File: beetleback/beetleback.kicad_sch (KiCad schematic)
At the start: 12 parts, among them J1 Conn_01x01_Male, J2 Conn_01x03_Male, J3 Conn_01x01_Male, U1 TA6586, U2 ATtiny412-SS, U3 ME6214A33M3G

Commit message: beetle motor esc back
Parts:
- removed C3: 10uF, Capacitor_SMD:C_0805_2012Metric, symbol Device:C
- removed D1: LED, LED_SMD:LED_0603_1608Metric_Castellated, symbol Device:LED
- removed J1, J3: Conn_01x01_Male, Connector_Wire:SolderWire-2sqmm_1x01_D2mm_OD3.9mm, symbol Connector:Conn_01x01_Male
- removed R1, R2: 330R, Resistor_SMD:R_0603_1608Metric, symbol Device:R
- removed U1: TA6586, Package_DIP:DIP-8_W7.62mm, symbol beetleback:TA6586
- removed U2: ATtiny412-SS, Package_SO:SOIC-8_3.9x4.9mm_P1.27mm, symbol MCU_Microchip_ATtiny:ATtiny412-SS
- removed U3: ME6214A33M3G, Package_TO_SOT_SMD:SOT-23, symbol beetleback:ME6214A33M3G
- added C5, C6, C7, C8: 22uF 18v, Capacitor_SMD:C_1206_3216Metric, symbol Device:C
- added C9: 1uF, Capacitor_SMD:C_0603_1608Metric, symbol Device:C
- added D1: MM5Z5V1, Diode_SMD:D_SOD-523, symbol Device:D_Zener
- added J1: power in, Connector_JST:JST_XA_B02B-XASK-1-A_1x02_P2.50mm_Vertical, symbol Connector:Conn_01x02_Female
- added J3: motor_pad_1, Connector_Pin:Pin_D1.3mm_L11.0mm, symbol Connector:Conn_01x01_Female
- added J4: motor_pad_2, Connector_Pin:Pin_D1.3mm_L11.0mm, symbol Connector:Conn_01x01_Female
- added R1, R2: 1k, Resistor_SMD:R_0603_1608Metric, symbol Device:R_Small
- added R3: 1k 0.5W, Capacitor_SMD:C_0805_2012Metric, symbol Device:R_Small
- added U1: ATtiny13A-SS, Package_SO:SOIC-8_3.9x4.9mm_P1.27mm, symbol MCU_Microchip_ATtiny:ATtiny13A-SS
- added U2: DRV8848, Package_SO:TSSOP-16-1EP_4.4x5mm_P0.65mm, symbol Driver_Motor:DRV8848
- C1: value 10uF -> 2.2uF; footprint Capacitor_SMD:C_0805_2012Metric -> Capacitor_SMD:C_0603_1608Metric; LCSC C15850 -> (none)
- C2: value 100nF -> 2.2uF; footprint Capacitor_SMD:C_0805_2012Metric -> Capacitor_SMD:C_0603_1608Metric; LCSC C49678 -> (none)
- J2: value Conn_01x03_Male -> servo in
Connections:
- net GND: now also J2.3 (Pin_3), C5.2, C6.2, C7.2, C8.2, C9.2, D1.2 (A), J1.2 (Pin_2), U1.4 (GND), U2.13 (GND), U2.17 (PPAD), U2.3 (AISEN), U2.6 (BISEN); no longer J2.1 (Pin_1)
- net VBAT: now also C5.1, C6.1, C7.1, C8.1, C9.1, J1.1 (Pin_1), R3.1, U2.12 (VM); no longer C1.1, J2.2 (Pin_2)
- net VLOGIC renamed DRV_VREF
- net DRV_VREF: now also U2.11 (VREF), U2.14 (VINT)
- new net: J2.1 (Pin_1), R1.1
- new net +5V: C1.1, D1.1 (K), R2.1, R3.2, U1.8 (VCC)
- new net MOTOR_PAD_1: J3.1 (Pin_1), U2.2 (AOUT1), U2.7 (BOUT1)
- new net MOTOR_PAD_2: J4.1 (Pin_1), U2.4 (AOUT2), U2.5 (BOUT2)
- new net MOTOR_PWM_1: U1.6 (PB1), U2.9 (BIN1)
- new net MOTOR_PWM_2: U1.5 (PB0), U2.10 (BIN2)
- new net PWMIN: R1.2, U1.7 (PB2)
- new net ~FAULT: U1.2 (PB3), U2.8 (nFAULT)
- new net ~SLEEP: R2.2, U2.1 (nSLEEP)
- no-connect marks 2 -> 5
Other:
- note added: "(18v -5v) / 1kohm = 13mA"
- note added: "(18v -5v) / 330ohm = 39mA"
- note added: "Beetleweight motor back ESC"
- note added: "For parallel operation leave AIN1 and AIN2 NC"
- note added: "Power input 2-4S 6-18v"
- note added: "Regulation"
- note added: "Servo 5v power"
- note added: "Servo connector"
- note added: "VBAT decoupling"
- note added: "Zener diode regulates voltage approx 5v"
- note removed: "Maximum input voltage 14V. 3S pack max Minimum input voltage 3.6 because we need enough voltage for the regulator to regulate down"
- moved on the sheet: J2

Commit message: board update
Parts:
- added D2: Red LED, LED_SMD:LED_0603_1608Metric, symbol Device:LED
- added R4: 1k, Resistor_SMD:R_0603_1608Metric, symbol Device:R_Small
- C1, C2: value 2.2uF -> 2.2uF 25v; LCSC (none) -> C57895
- C5, C6, C7, C8: value 22uF 18v -> 22uF 25v; LCSC (none) -> C5672
- C9: value 1uF -> 2.2uF 25v; LCSC (none) -> C57895
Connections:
- net GND: now also D2.1 (K)
- net at U1.3 (PB4): now also R4.1
- new net: D2.2 (A), R4.2
- no-connect marks 5 -> 4

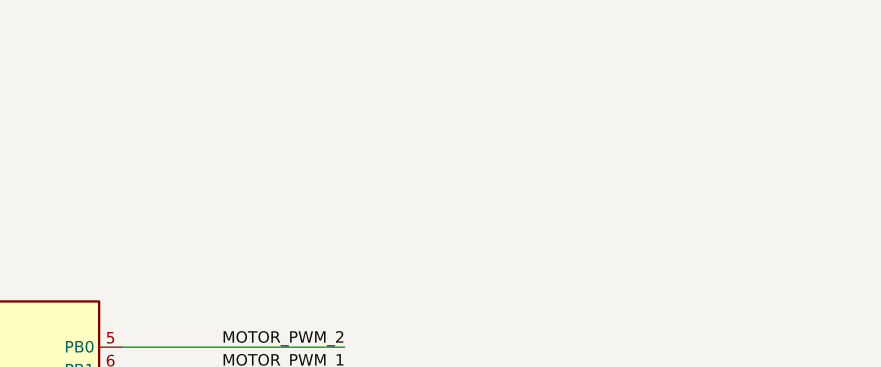
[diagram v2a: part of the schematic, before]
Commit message: Beetleweight motor back esc
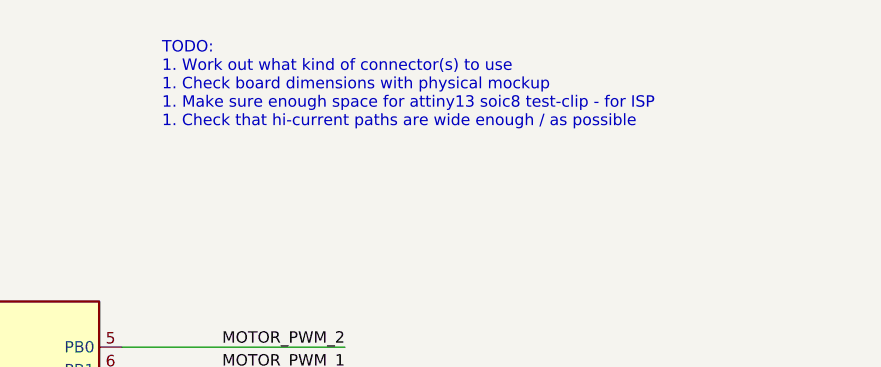
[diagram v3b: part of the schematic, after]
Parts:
- J3, J4: footprint Connector_Pin:Pin_D1.3mm_L11.0mm -> beetleback:bbb_motorpin
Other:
- note added: "TODO: 1. Work out what kind of connector(s) to use 1. Check board dimensions with physical mockup 1. Make sure enough space for attiny13 soic8 test-clip - for ISP 1. Check that hi-current paths are wide enough / as possible"
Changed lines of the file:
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@@
 (kicad_sch (version 20201015) (generator eeschema)
-  (page 1 1)
   (paper "A4")
   (title_block
@@
   (junction (at 201.93 120.65) (diameter 1.016) (color 0 0 0 0))
   (junction (at 206.375 133.35) (diameter 1.016) (color 0 0 0 0))
+  (no_connect (at 165.1 125.73))
+  (no_connect (at 196.85 68.58))
+  (no_connect (at 44.45 50.8))
   (no_connect (at 165.1 128.27))
-  (no_connect (at 165.1 125.73))
-  (no_connect (at 44.45 50.8))
-  (no_connect (at 196.85 68.58))
   (wire (pts (xy 27.94 128.27) (xy 46.99 128.27))
     (stroke (width 0) (type solid) (color 0 0 0 0))
@@
   (text "Beetleweight motor back ESC" (at 175.26 26.035 180)
     (effects (font (size 4 4)) (justify right bottom))
+  )
+  (text "TODO:\n1. Work out what kind of connector(s) to use\n1. Check board dimensions with physical mockup\n1. Make sure enough space for attiny13 soic8 test-clip - for ISP\n1. Check that hi-current paths are wide enough / as possible\n\n"
+    (at 201.295 33.655 0)
+    (effects (font (size 1.27 1.27)) (justify left bottom))
   )
   (label "VBAT" (at 32.385 171.45 0)
@@
       (effects (font (size 1.27 1.27)) (justify left))
     )
-    (property "Footprint" "Connector_Pin:Pin_D1.3mm_L11.0mm" (id 2) (at 248.285 120.65 0)
+    (property "Footprint" "beetleback:bbb_motorpin" (id 2) (at 248.285 120.65 0)
       (effects (font (size 1.27 1.27)) hide)
     )
@@
       (effects (font (size 1.27 1.27)) (justify left))
     )
-    (property "Footprint" "Connector_Pin:Pin_D1.3mm_L11.0mm" (id 2) (at 248.285 133.35 0)
+    (property "Footprint" "beetleback:bbb_motorpin" (id 2) (at 248.285 133.35 0)
       (effects (font (size 1.27 1.27)) hide)
     )
@@
     )
     (path "/13b79033-d552-42ca-ba14-db71e8ae705b"
-      (reference "J3") (unit 1) (value "motor_pad_1") (footprint "Connector_Pin:Pin_D1.3mm_L11.0mm")
+      (reference "J3") (unit 1) (value "motor_pad_1") (footprint "beetleback:bbb_motorpin")
     )
     (path "/329a2388-d6e0-461d-a82a-7749a2ecf868"
-      (reference "J4") (unit 1) (value "motor_pad_2") (footprint "Connector_Pin:Pin_D1.3mm_L11.0mm")
+      (reference "J4") (unit 1) (value "motor_pad_2") (footprint "beetleback:bbb_motorpin")
     )
     (path "/66241c81-47d1-4787-abff-1a86cfe19362"

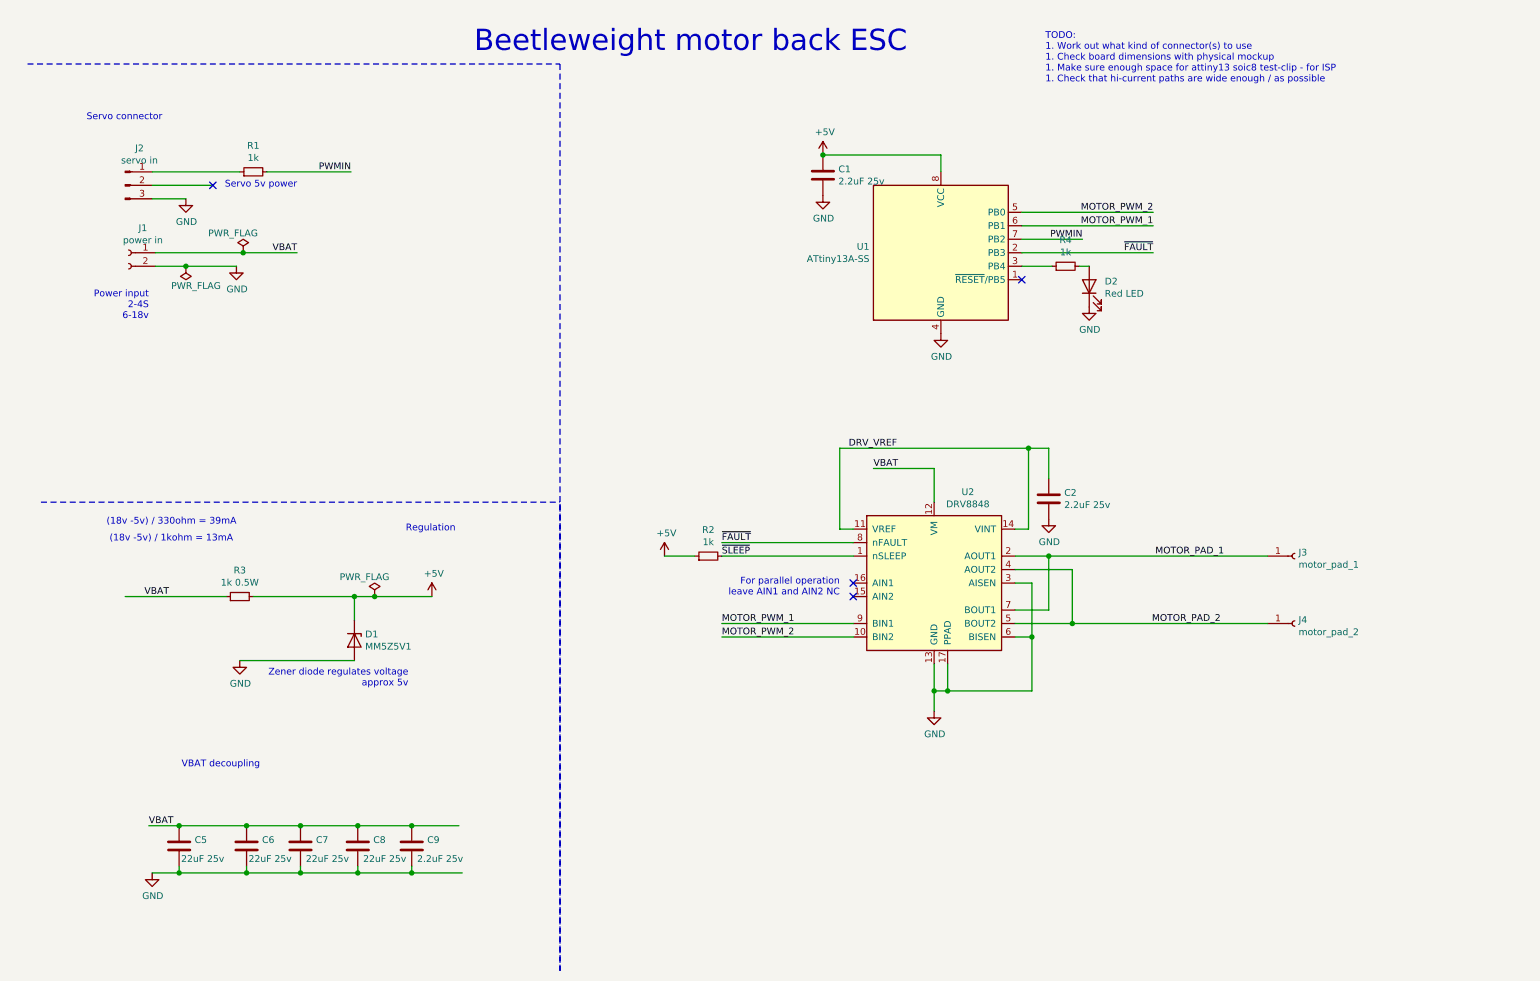
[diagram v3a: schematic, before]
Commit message: Use double sided jst; add bbb logo
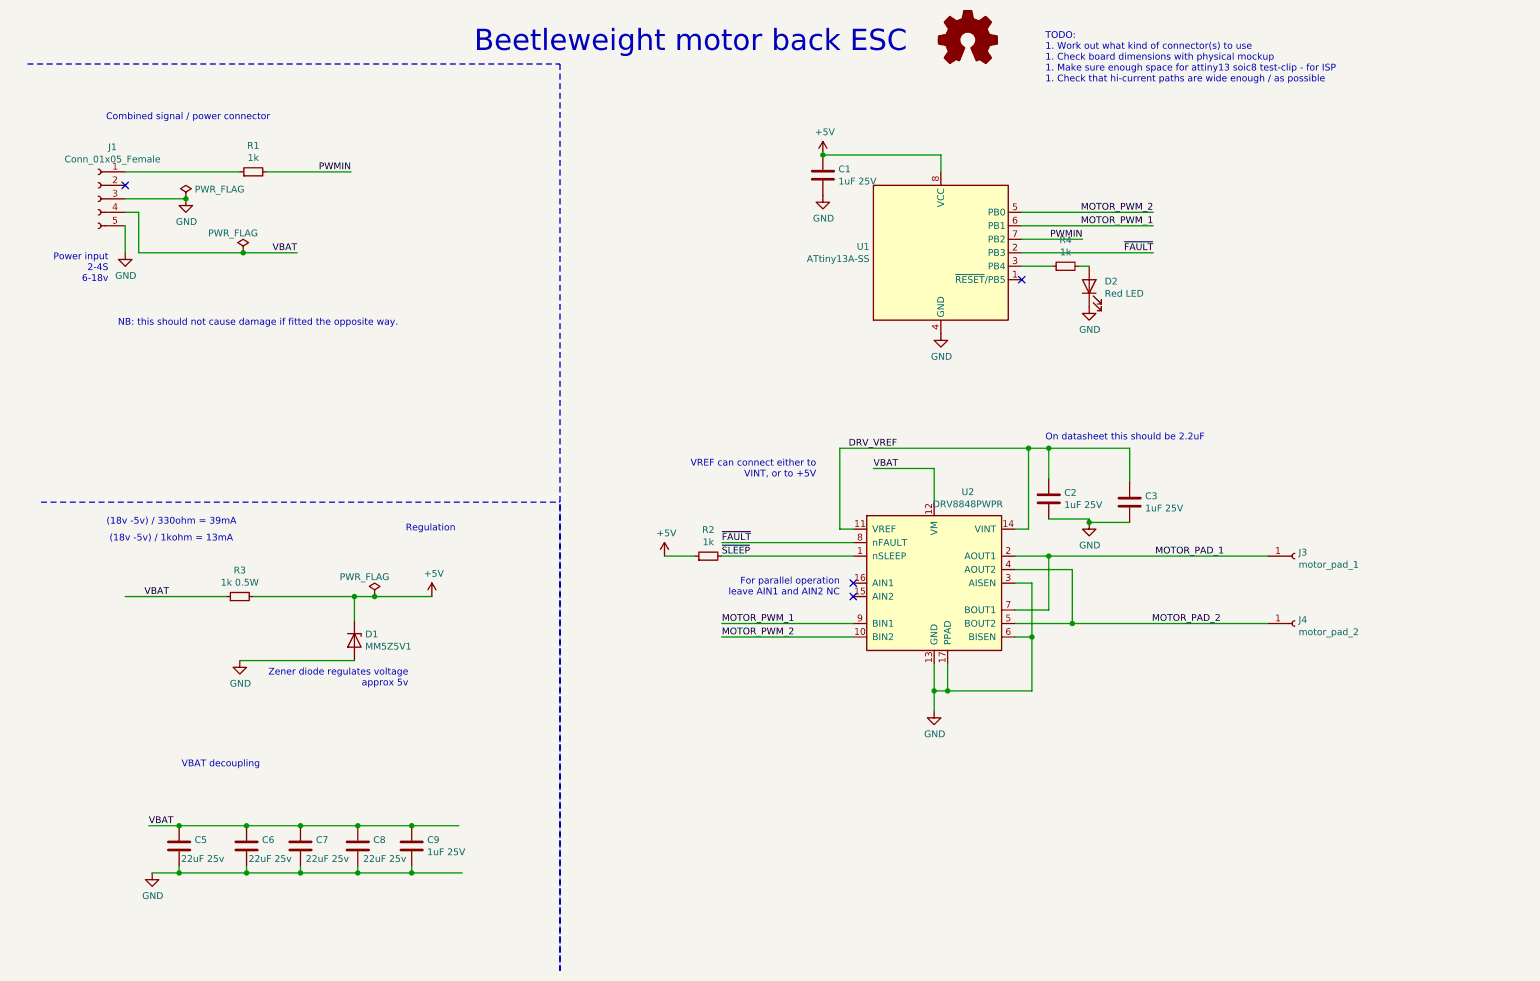
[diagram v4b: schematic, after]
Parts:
- removed J1: power in, Connector_JST:JST_XA_B02B-XASK-1-A_1x02_P2.50mm_Vertical, symbol Connector:Conn_01x02_Female
- removed J2: servo in, Connector_PinHeader_2.54mm:PinHeader_1x03_P2.54mm_Vertical, symbol Connector:Conn_01x03_Male
- added C3: 1uF 25V, Capacitor_SMD:C_0402_1005Metric, symbol Device:C
- added J1: Conn_01x05_Female, beetleback:JST_XH_B5B-XH-AM_doubleside, symbol Connector:Conn_01x05_Female
- C1, C2, C9: value 2.2uF 25v -> 1uF 25V; footprint Capacitor_SMD:C_0603_1608Metric -> Capacitor_SMD:C_0402_1005Metric; LCSC C57895 -> C52923
- C5, C6, C7, C8: LCSC C5672 -> (none)
- D2: LCSC (none) -> C2286
- R1, R2, R4: LCSC (none) -> C21190
- R3: footprint Capacitor_SMD:C_0805_2012Metric -> Resistor_SMD:R_0805_2012Metric
- U1: LCSC (none) -> C40382
- U2: value DRV8848 -> DRV8848PWPR; LCSC (none) -> C131079
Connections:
- net DRV_VREF: now also C3.1
- net GND: now also C3.2, J1.3 (Pin_3), J1.5 (Pin_5)
- net VBAT: now also J1.4 (Pin_4)
- net at R1.1: now also J1.1 (Pin_1)
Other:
- note added: "Combined signal / power connector"
- note added: "NB: this should not cause damage if fitted the opposite way."
- note added: "On datasheet this should be 2.2uF"
- note added: "VREF can connect either to VINT, or to +5V"
- note removed: "Servo 5v power"
- note removed: "Servo connector"

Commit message: Use 4-layer board
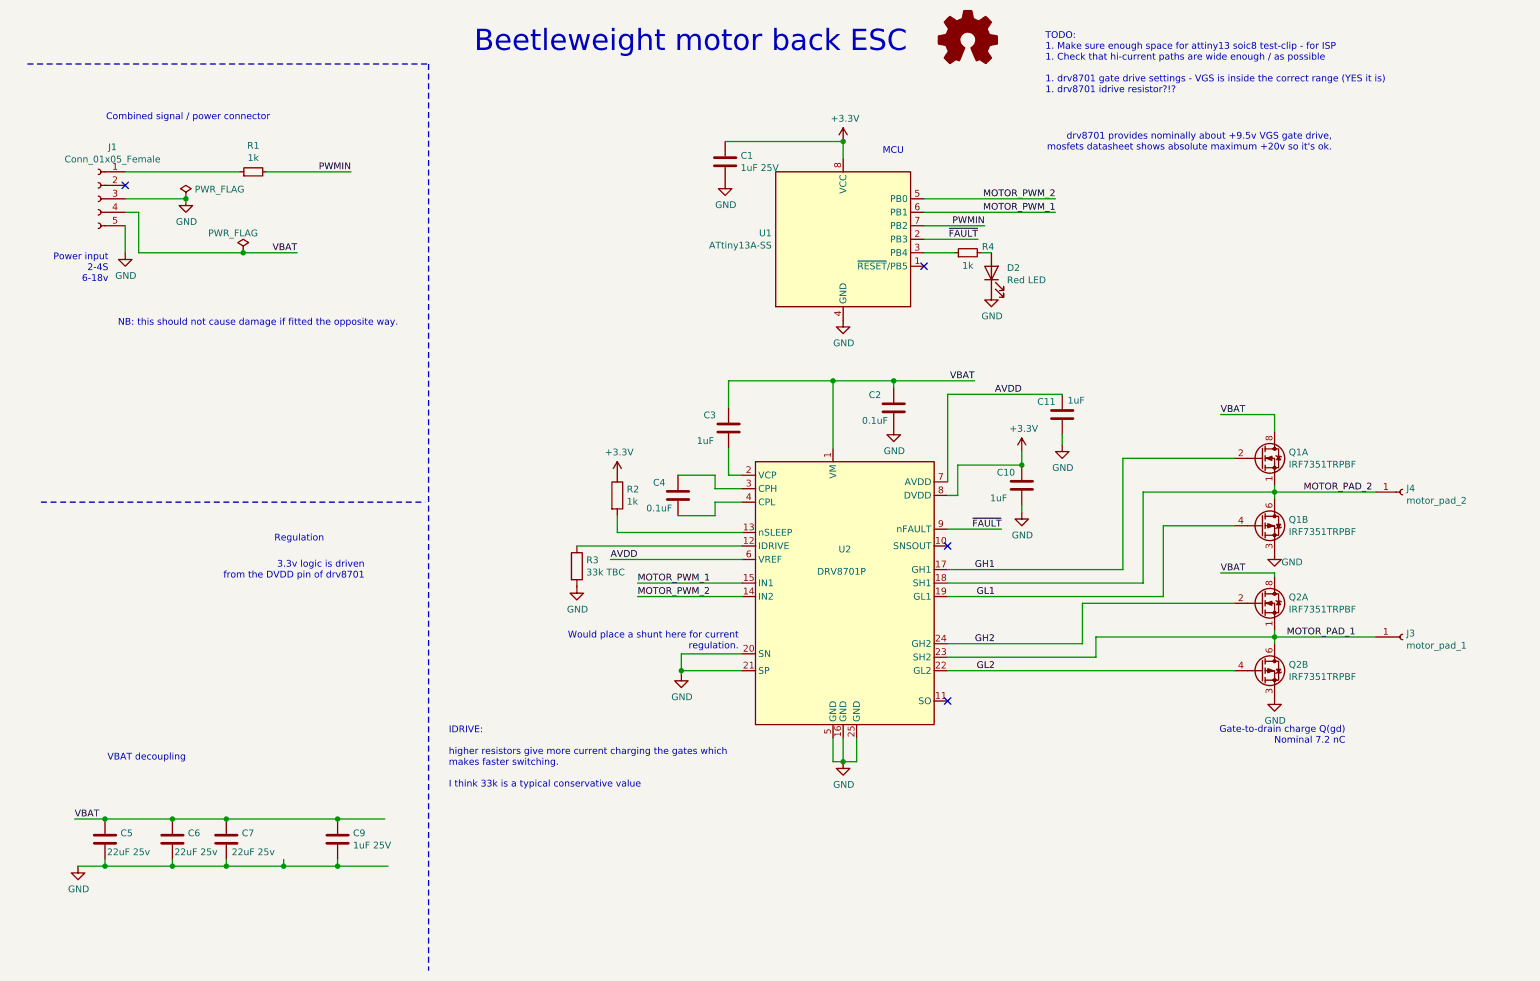
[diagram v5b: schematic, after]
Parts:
- removed C8: 22uF 25v, Capacitor_SMD:C_1206_3216Metric, symbol Device:C
- removed D1: MM5Z5V1, Diode_SMD:D_SOD-523, symbol Device:D_Zener
- removed R2: 1k, Resistor_SMD:R_0603_1608Metric, symbol Device:R_Small
- removed R3: 1k 0.5W, Resistor_SMD:R_0805_2012Metric, symbol Device:R_Small
- removed U2: DRV8848PWPR, Package_SO:TSSOP-16-1EP_4.4x5mm_P0.65mm, symbol Driver_Motor:DRV8848
- added C10, C11: 1uF, Capacitor_SMD:C_0402_1005Metric, symbol Device:C
- added C4: 0.1uF, Capacitor_SMD:C_0402_1005Metric, symbol Device:C
- added Q1, Q2: IRF7351TRPBF, Package_SO:SOIC-8_3.9x4.9mm_P1.27mm, symbol Transistor_FET:IRF7343PBF
- added R2: 1k, Resistor_SMD:R_0402_1005Metric, symbol Device:R
- added R3: 33k TBC, Resistor_SMD:R_0402_1005Metric, symbol Device:R
- added U2: DRV8701P, Package_DFN_QFN:VQFN-24-1EP_4x4mm_P0.5mm_EP2.45x2.45mm, symbol beetleback:DRV8701P
- C2: value 1uF 25V -> 0.1uF; LCSC C52923 -> (none)
- C3: value 1uF 25V -> 1uF; LCSC C52923 -> (none)
- C5, C6, C7: LCSC (none) -> C12891
- R1, R4: footprint Resistor_SMD:R_0603_1608Metric -> Resistor_SMD:R_0402_1005Metric
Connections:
- net DRV_VREF is gone; now on net VBAT: C2.1, C3.1
- net GND: now also C10.2, C11.2, Q1.3 (1), Q2.3 (1), R3.2, U2.16 (GND), U2.20 (SN), U2.21 (SP), U2.25 (GND), U2.5 (GND); no longer C3.2
- net MOTOR_PAD_1: now also Q2.1 (S), Q2.5 (D), Q2.6 (D), U2.23 (SH2)
- net MOTOR_PAD_2: now also Q1.1 (S), Q1.5 (D), Q1.6 (D), U2.18 (SH1)
- net MOTOR_PWM_1: now also U2.15 (IN1)
- net MOTOR_PWM_2: now also U2.14 (IN2)
- net VBAT: now also Q1.7 (D), Q1.8 (D), Q2.7 (D), Q2.8 (D), U2.1 (VM)
- net ~FAULT: now also U2.9 (nFAULT)
- net +5V renamed +3V3
- net +3V3: now also C10.1, R2.1, U2.8 (DVDD)
- new net: R2.2, U2.13 (nSLEEP)
- new net: R3.1, U2.12 (IDRIVE)
- new net: C3.2, U2.2 (VCP)
- new net: C4.1, U2.3 (CPH)
- new net: C4.2, U2.4 (CPL)
- new net AVDD: C11.1, U2.6 (VREF), U2.7 (AVDD)
- new net GH1: Q1.2 (G), U2.17 (GH1)
- new net GH2: Q2.2 (G), U2.24 (GH2)
- new net GL1: Q1.4 (G), U2.19 (GL1)
- new net GL2: Q2.4 (G), U2.22 (GL2)
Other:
- note added: "3.3v logic is driven from the DVDD pin of drv8701"
- note added: "Gate-to-drain charge Q(gd) Nominal 7.2 nC"
- note added: "IDRIVE: higher resistors give more current charging the gates which makes faster switching. I think 33k is a typical conservative value"
- note added: "MCU"
- note added: "TODO: 1. Make sure enough space for attiny13 soic8 test-clip - for ISP 1. Check that hi-current paths are wide enough / as possible 1. drv8701 gate drive settings - VGS is inside the correct range (YES it is) 1. drv8701 idrive resistor?!?"
- note added: "Would place a shunt here for current regulation."
- note added: "drv8701 provides nominally about +9.5v VGS gate drive, mosfets datasheet shows absolute maximum +20v so it's ok."
- note removed: "(18v -5v) / 1kohm = 13mA"
- note removed: "(18v -5v) / 330ohm = 39mA"
- note removed: "For parallel operation leave AIN1 and AIN2 NC"
- note removed: "On datasheet this should be 2.2uF"
- note removed: "TODO: 1. Work out what kind of connector(s) to use 1. Check board dimensions with physical mockup 1. Make sure enough space for attiny13 soic8 test-clip - for ISP 1. Check that hi-current paths are wide enough / as possible"
- note removed: "VREF can connect either to VINT, or to +5V"
- note removed: "Zener diode regulates voltage approx 5v"
- moved on the sheet: C1, C5, C6, C7, C9, D2, J3, J4, R4, U1
